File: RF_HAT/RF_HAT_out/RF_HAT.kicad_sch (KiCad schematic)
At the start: 0 parts

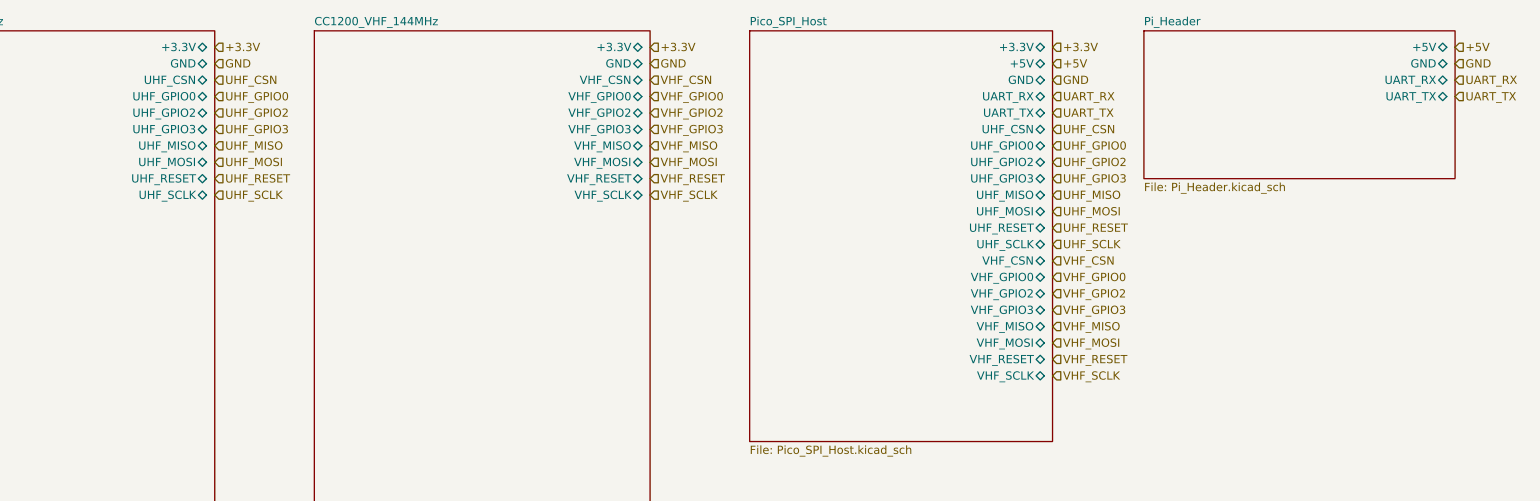
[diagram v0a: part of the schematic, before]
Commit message: switch to SMD pico
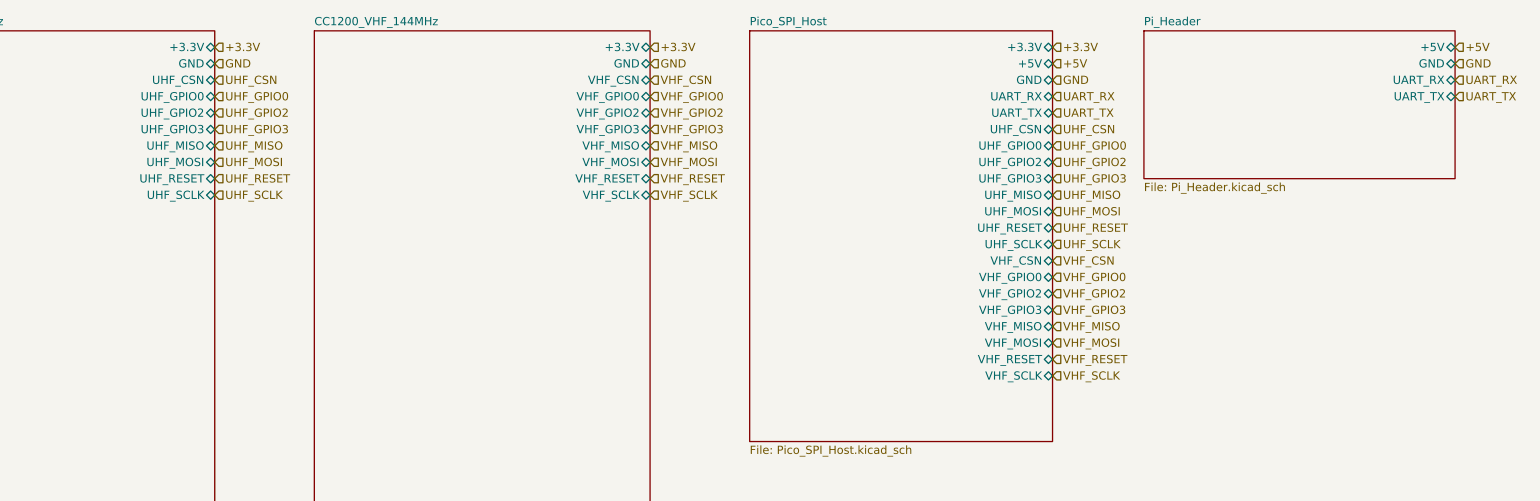
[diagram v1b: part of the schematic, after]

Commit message: first routing of signals
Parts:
- added H1, H2, H3, H4: MountingHole_Pad, MountingHole:MountingHole_2.7mm_M2.5_ISO14580_Pad, symbol Mechanical:MountingHole_Pad
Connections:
- net GND: now also H1.1, H2.1, H3.1, H4.1

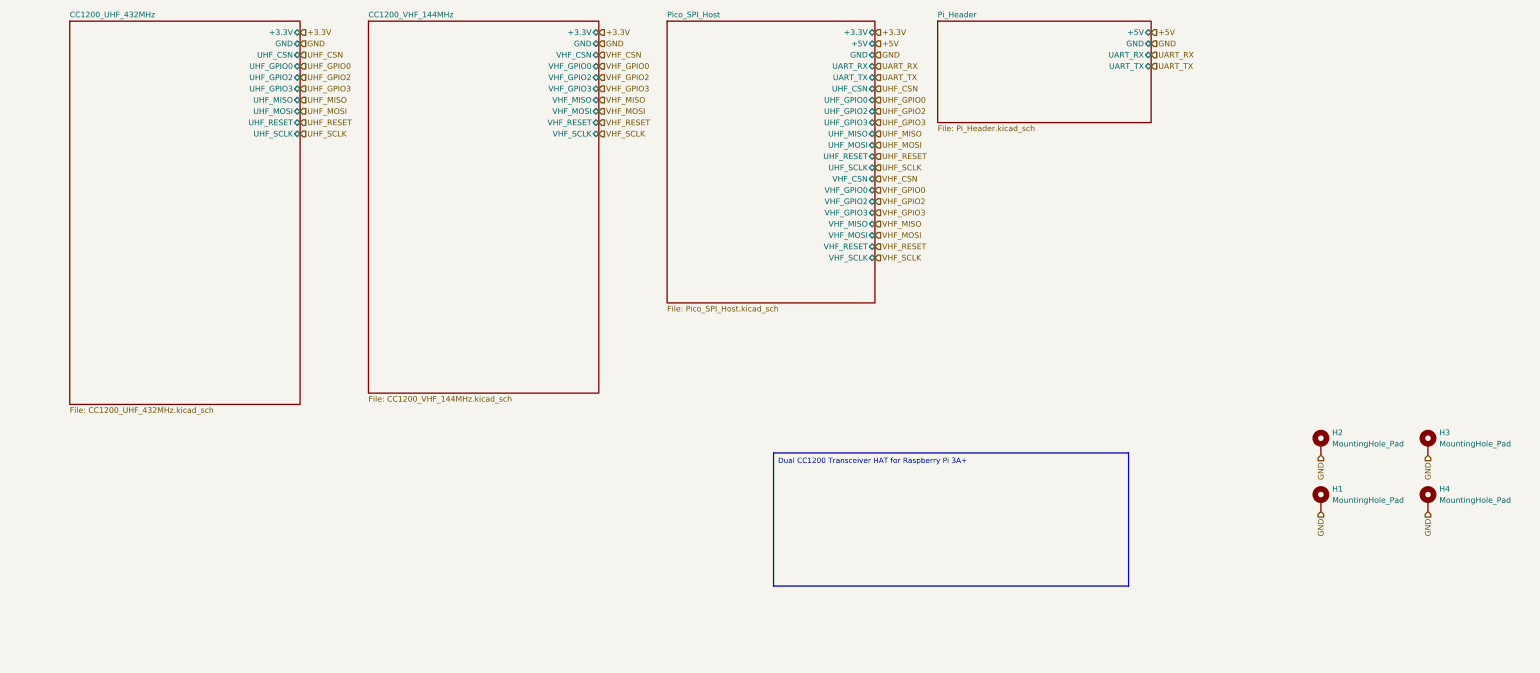
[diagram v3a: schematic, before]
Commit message: Restructured kicad schematic for CC1200 PI_HAT readablitity based on M17 reference schematics
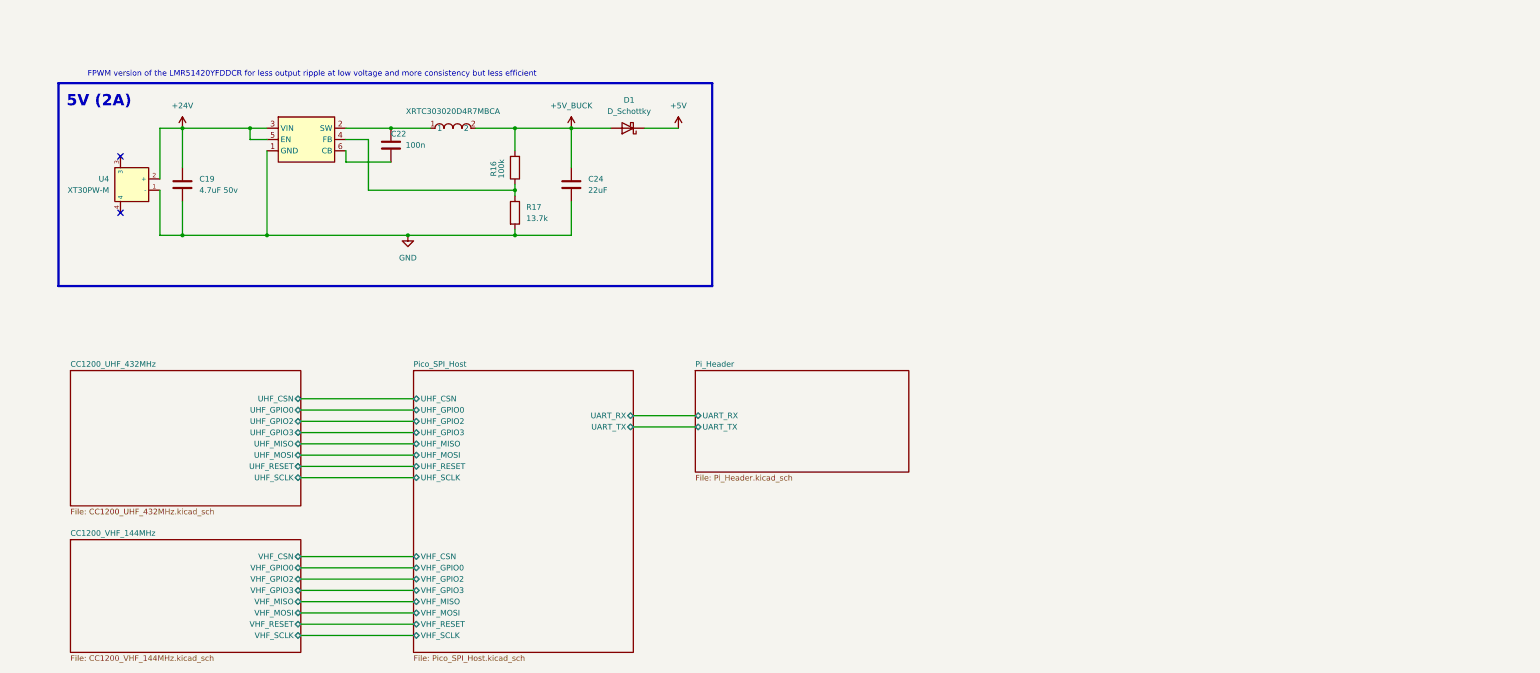
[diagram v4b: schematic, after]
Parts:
- removed H1, H2, H3, H4: MountingHole_Pad, MountingHole:MountingHole_2.7mm_M2.5_ISO14580_Pad, symbol Mechanical:MountingHole_Pad
- added C19: 4.7uF 50v, Capacitor_SMD:C_0805_2012Metric, symbol Device:C
- added C22: 100n, Capacitor_SMD:C_0603_1608Metric, symbol Device:C
- added C24: 22uF, Capacitor_SMD:C_0603_1608Metric, symbol Device:C
- added D1: D_Schottky, Diode_SMD:D_0603_1608Metric, symbol Device:D_Schottky
- added L18: XRTC303020D4R7MBCA, lib:IND-SMD_L3.0-W3.0_AFE303020S, symbol lib:XRTC303020D4R7MBCA
- added R16: 100k, Capacitor_SMD:C_0603_1608Metric, symbol Device:R
- added R17: 13.7k, Capacitor_SMD:C_0603_1608Metric, symbol Device:R
- added U4: XT30PW-M, Connector_AMASS:AMASS_XT30PW-M_1x02_P2.50mm_Horizontal, symbol components:XT30PW-M
- added U5: LMR51420YFDDCR, lib:SOT-23-6_L2.9-W1.6-P0.95-LS2.9-BL, symbol lib:LMR51420YDDCR
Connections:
- net +5V: now also D1.1 (K)
- net GND: now also C19.2, C24.2, R17.2, U4.1 (-), U5.1 (GND)
- new net: R16.1, R17.1, U5.4 (FB)
- new net: C22.1, L18.1, U5.2 (SW)
- new net: C22.2, U5.6 (CB)
- new net +24V: C19.1, U4.2 (+), U5.3 (VIN), U5.5 (EN)
- new net +5V_BUCK: C24.1, D1.2 (A), L18.2, R16.2
- no-connect marks 0 -> 2
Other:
- sheet CC1200_UHF_432MHz ports: added none; removed +3.3V, GND
- sheet CC1200_VHF_144MHz ports: added none; removed +3.3V, GND
- sheet Pi_Header ports: added none; removed +5V, GND
- sheet Pico_SPI_Host ports: added none; removed +3.3V, +5V, GND
- note added: "5V (2A)"
- note added: "FPWM version of the LMR51420YFDDCR for less output ripple at low voltage and more consistency but less efficient"

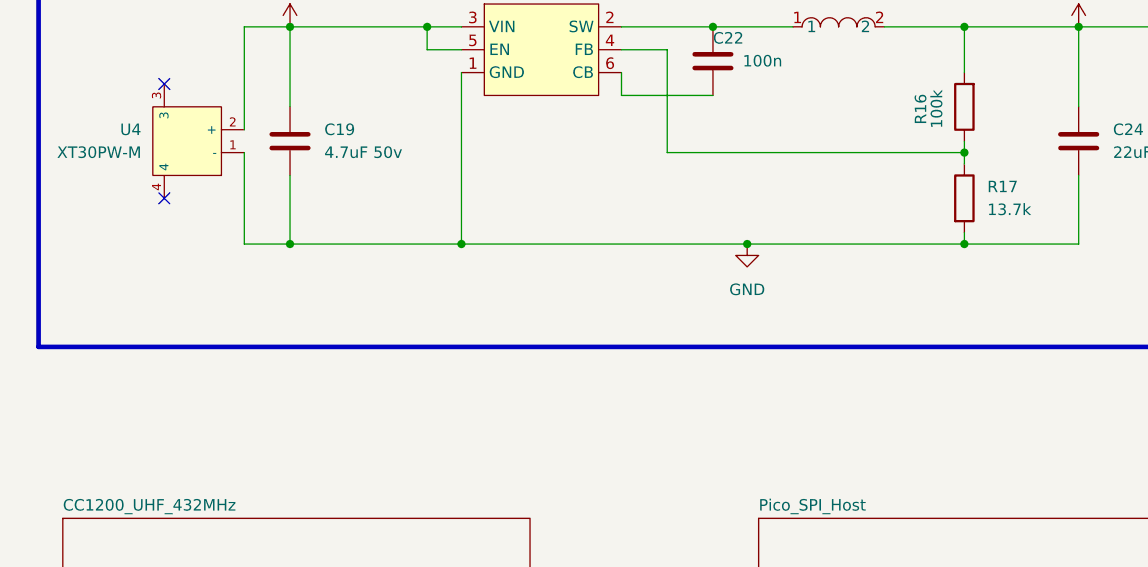
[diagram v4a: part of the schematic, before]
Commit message: added board edge and connector placement
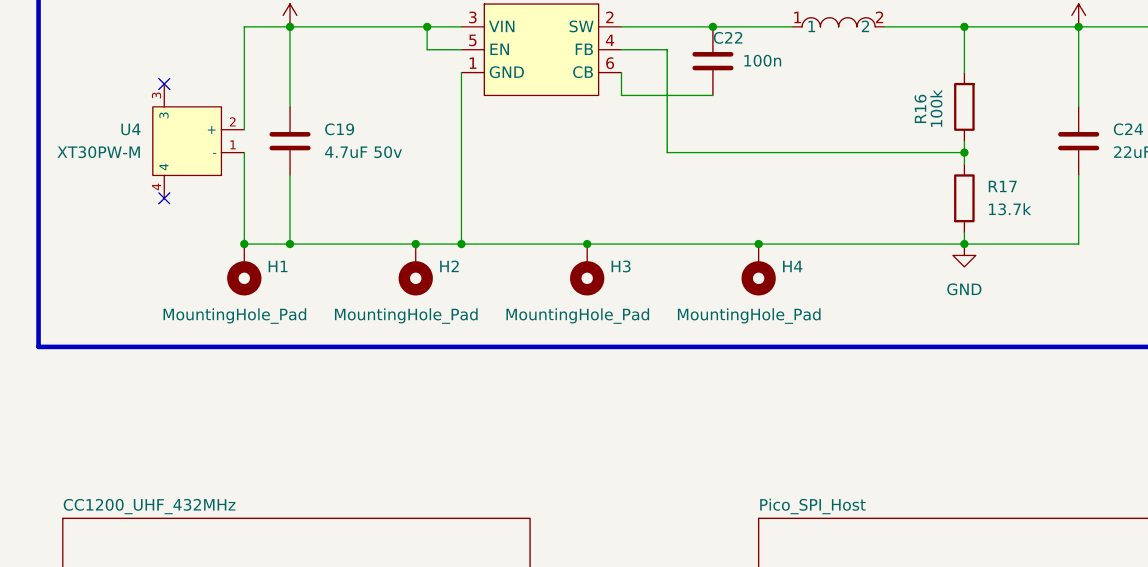
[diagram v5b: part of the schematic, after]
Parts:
- added H1, H2, H3, H4: MountingHole_Pad, MountingHole:MountingHole_2.7mm_M2.5_ISO7380_Pad, symbol Mechanical:MountingHole_Pad
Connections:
- net GND: now also H1.1, H2.1, H3.1, H4.1

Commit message: did final routing and added Farnell and LCSC numbers to all components
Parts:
- C19: Farnell (none) -> 1735545
- C22: Farnell (none) -> 1650835
- C24: Farnell (none) -> 4292940
- D1: Farnell (none) -> 1843687; LCSC (none) -> C3759853
- L18: Farnell (none) -> 4142875; LCSC (none) -> C39846837
- R16: Farnell (none) -> 9238727
- R17: Farnell (none) -> 2138429
- U5: LCSC (none) -> C7296200

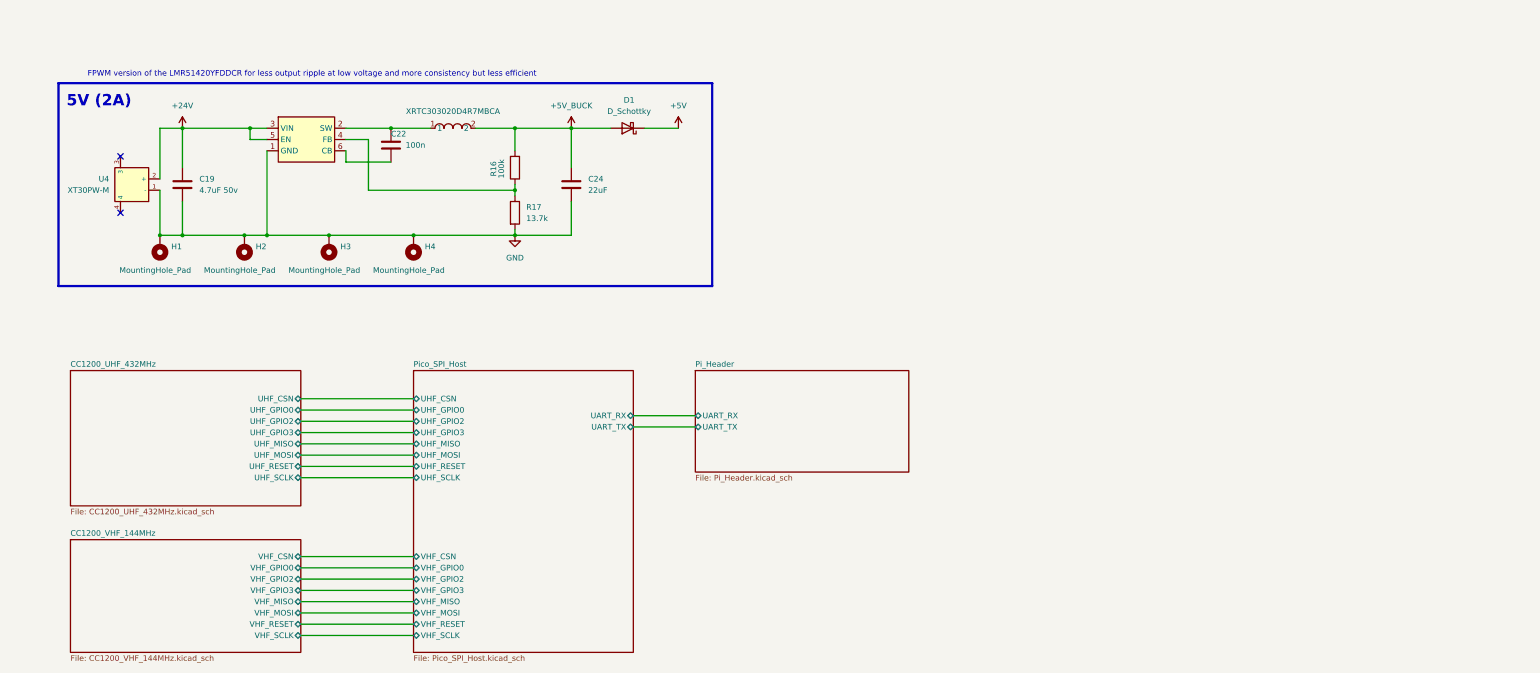
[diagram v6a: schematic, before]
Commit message: update RF_HAT to have WS2812 and buzzer. Start on webserver interface with demo visuals, integration in satnogs system, dual SPI and UART to USB on the Pi_HAT, update readme's
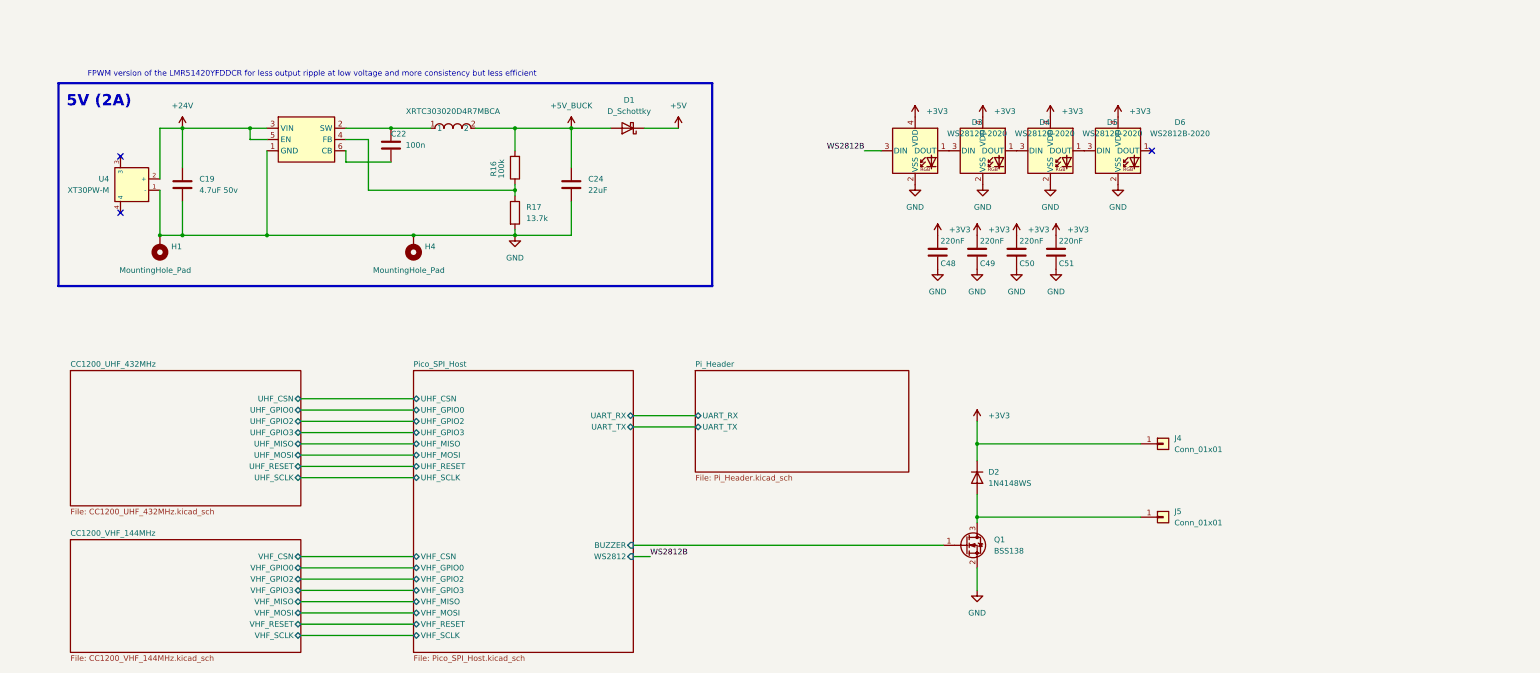
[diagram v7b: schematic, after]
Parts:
- removed H2, H3: MountingHole_Pad, MountingHole:MountingHole_2.7mm_M2.5_ISO7380_Pad, symbol Mechanical:MountingHole_Pad
- added C48, C49, C50, C51: 220nF, Capacitor_SMD:C_0603_1608Metric, symbol Device:C
- added D2: 1N4148WS, Diode_SMD:D_SOD-323, symbol Diode:1N4148WS
- added D3, D4, D5, D6: WS2812B-2020, LED_SMD:LED_WS2812B-2020_PLCC4_2.0x2.0mm, symbol LED:WS2812B-2020
- added J4, J5: Conn_01x01, Connector_PinHeader_2.00mm:PinHeader_1x01_P2.00mm_Vertical, symbol Connector_Generic:Conn_01x01
- added Q1: BSS138, Package_TO_SOT_SMD:SOT-23, symbol Transistor_FET:BSS138
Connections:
- net GND: now also C48.2, C49.2, C50.2, C51.2, D3.2 (VSS), D4.2 (VSS), D5.2 (VSS), D6.2 (VSS), Q1.2 (S)
- new net: D5.1 (DOUT), D6.3 (DIN)
- new net: D4.1 (DOUT), D5.3 (DIN)
- new net: D3.1 (DOUT), D4.3 (DIN)
- new net: D2.2 (A), J5.1 (Pin_1), Q1.3 (D)
- new net +3V3: C48.1, C49.1, C50.1, C51.1, D2.1 (K), D3.4 (VDD), D4.4 (VDD), D5.4 (VDD), D6.4 (VDD), J4.1 (Pin_1)
- new net Pico_SPI_Host/BUZZER: Q1.1 (G)
- new net WS2812B: D3.3 (DIN)
- no-connect marks 2 -> 3
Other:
- sheet Pico_SPI_Host ports: added BUZZER, WS2812; removed none
